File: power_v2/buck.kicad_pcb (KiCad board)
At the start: 4 copper layers, 113.5 x 84 mm, 50 parts, among them J1 Conn_01x01, J2 Conn_01x01, Q1 Q_PMOS_GDS, U1 LTC2946CMS#PBF

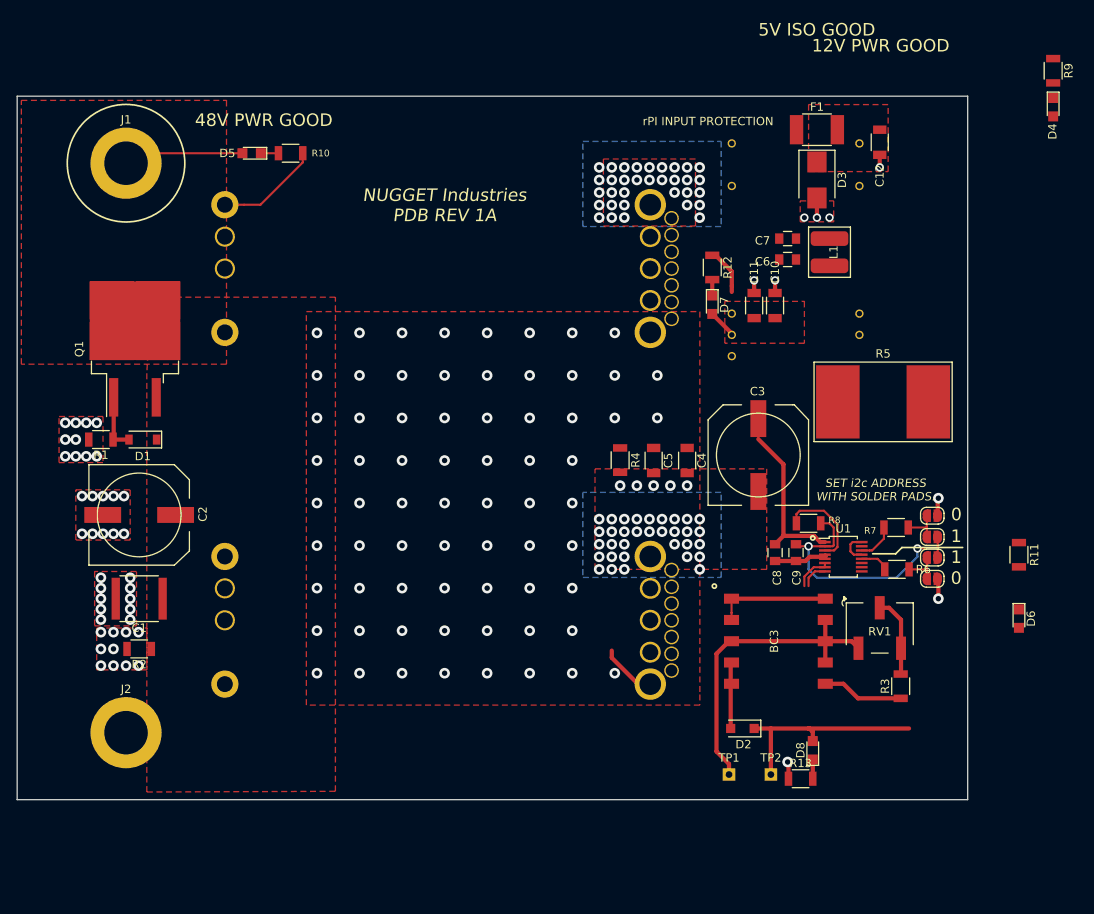
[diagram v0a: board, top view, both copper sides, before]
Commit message: PCA symbol moved to sensor board
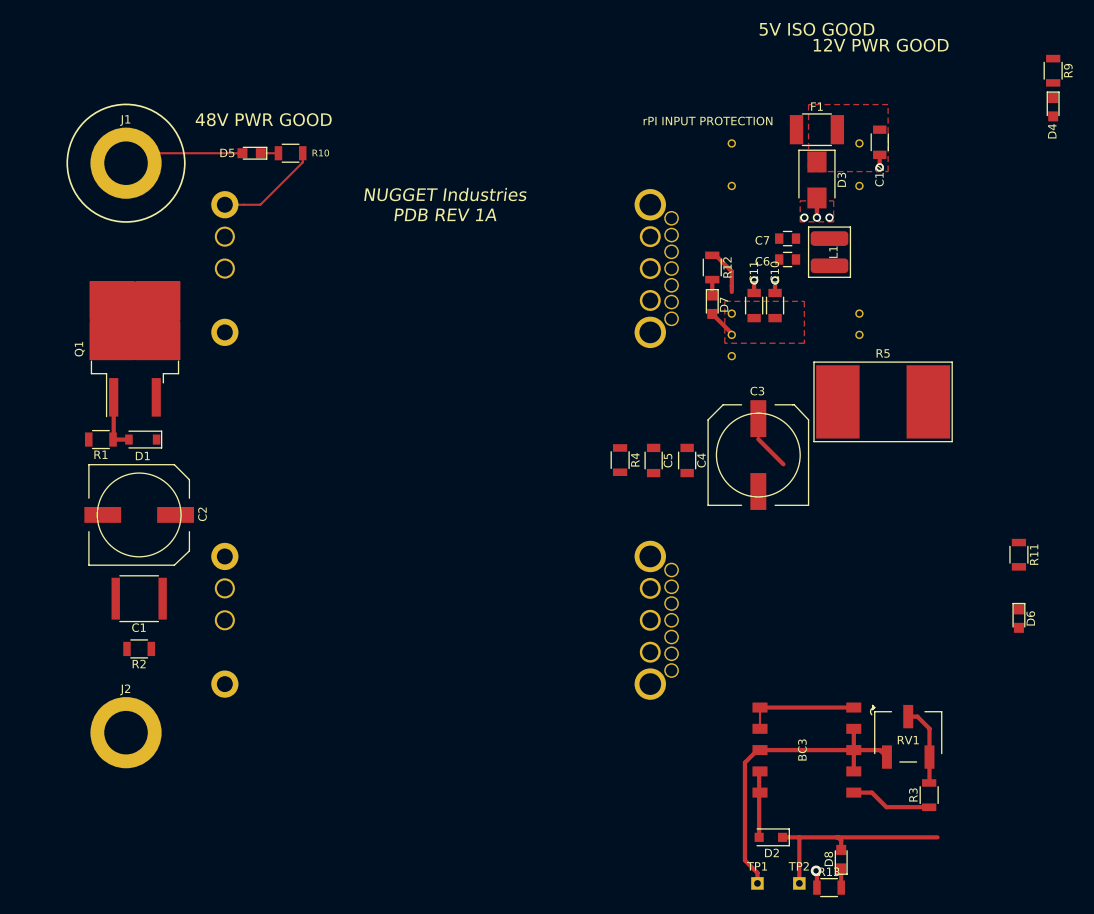
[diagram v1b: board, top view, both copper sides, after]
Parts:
- removed C8, C9: .1uF, Capacitors_SMD:C_0805
- removed JP1, JP2, JP3, JP4: SolderJumper_2_Open, jumpers:SolderJumper-2_P1.3mm_Open_RoundedPad1.0x1.5mm
- removed R6, R7: 22K, Resistors_SMD:R_1206
- removed R8: 4.7K, Resistors_SMD:R_1206
- removed U1: LTC2946CMS#PBF, Housings_SSOP:MSOP-16_3x4mm_Pitch0.5mm
- moved D2 13.4 mm to (105.0, 108.5)
- moved D8 13.4 mm to (113.4, 111.1)
- moved R13 13.4 mm to (112.0, 114.5)
- moved R3 13.4 mm to (123.9, 103.5)
- moved RV1 13.4 mm to (121.4, 96.5)
- moved TP1 13.4 mm to (103.4, 114.0)
- moved TP2 13.4 mm to (108.4, 114.0)
- moved BC3 13.4 mm to (109.3, 98.1)
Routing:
- net /INTVCC: track 31.6 -> 0.00 mm, vias 2 -> 0
- net /VOUT: track 32.5 -> 8.15 mm, vias 69 -> 0
- net /GP_OUTPUT: track 11.2 -> 0.00 mm
- net GNDPWR: track 51.0 -> 40.1 mm, vias 74 -> 1
- net Net-(JP3-Pad2): track 4.76 -> 0.00 mm
- net Net-(JP1-Pad2): track 4.66 -> 0.00 mm
- net /ADR1: track 4.56 -> 0.00 mm
- net /SDAISO: track 4.56 -> 0.00 mm
- net /ADR0: track 3.51 -> 0.00 mm
- net /SCLISO: track 3.26 -> 0.00 mm
- net Earth: vias 40 -> 0
- removed copper zone on F.Cu, net +48V
- removed copper zone on F.Cu, net /VIN+
- removed copper zone on F.Cu, net /VOUT
- removed copper zone on F.Cu, net Earth
- removed copper zone on B.Cu, net GNDPWR
- removed copper zone on F.Cu, net GNDPWR
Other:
- board outline removed
- board text removed: "0"
- board text removed: "1"
- board text removed: "SET i2c ADDRESS WITH SOLDER PADS."
